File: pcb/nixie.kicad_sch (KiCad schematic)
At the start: 2 parts

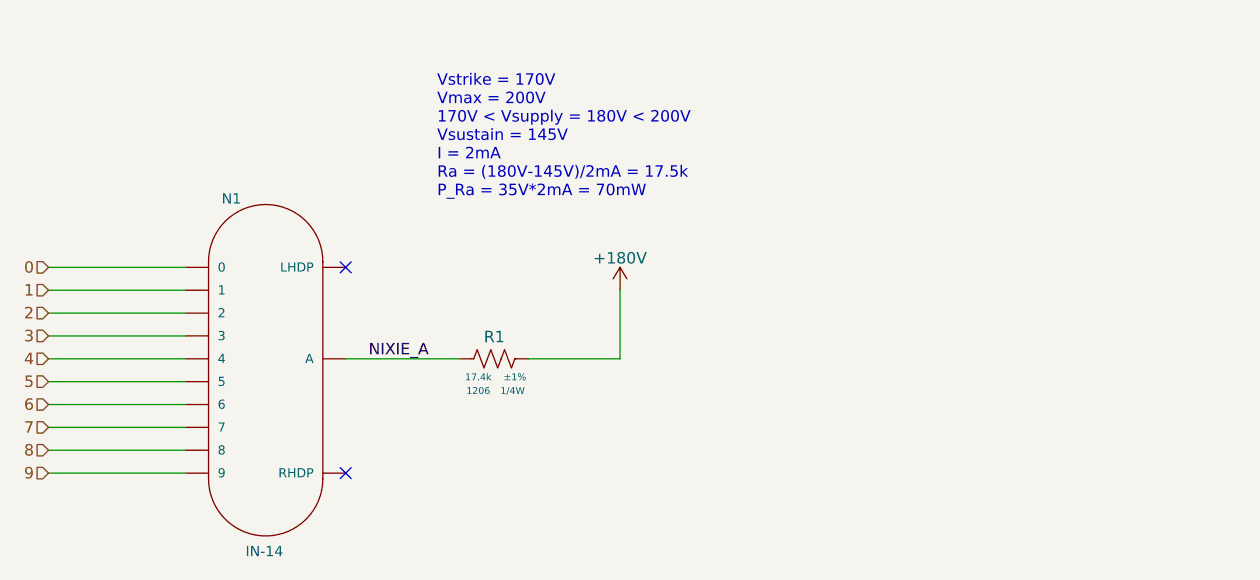
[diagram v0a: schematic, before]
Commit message: Added LSE crystal and started configuring MCU Pinout"
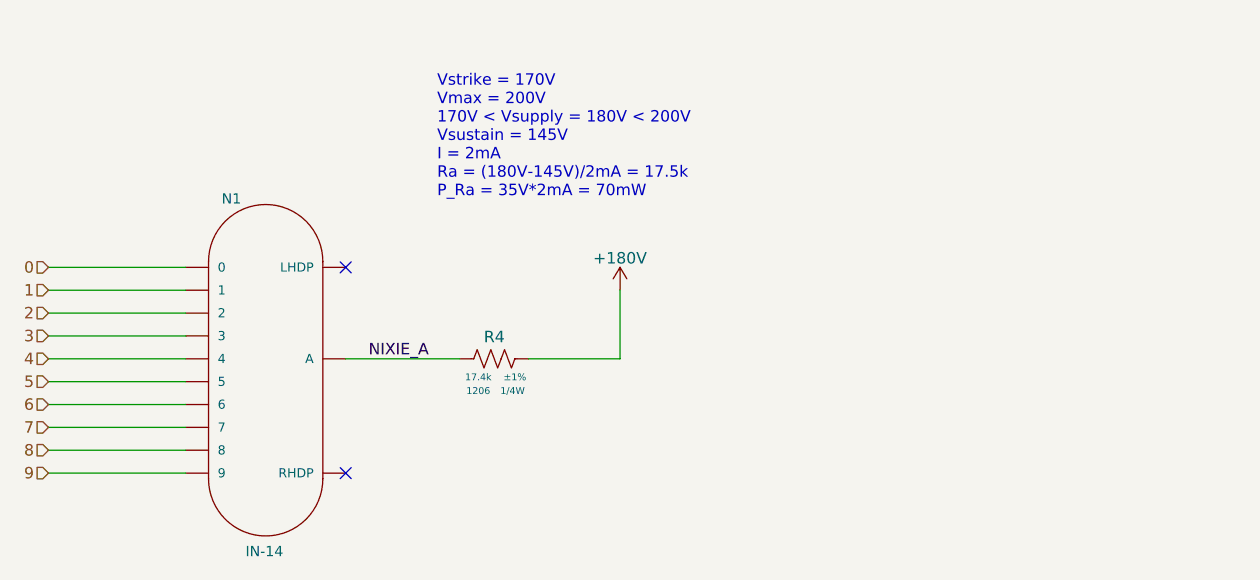
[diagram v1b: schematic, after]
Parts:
- renumbered R1 to R4
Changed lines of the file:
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@@
   (symbol (lib_id "arjun_symbols:RES_17K4_1P_1{slash}4W_1206") (at 170.18 101.6 270) (unit 1)
     (in_bom yes) (on_board yes)
-    (property "Reference" "R1" (id 0) (at 166.37 98.425 90)
+    (property "Reference" "R4" (id 0) (at 166.37 98.425 90)
       (effects (font (size 1.27 1.27)) (justify top))
     )
@@
   (symbol (lib_id "arjun_symbols:+180V") (at 180.34 93.98 0) (unit 1)
     (in_bom yes) (on_board yes)
-    (property "Reference" "#PWR06" (id 0) (at 180.34 97.79 0)
+    (property "Reference" "#PWR015" (id 0) (at 180.34 97.79 0)
       (effects (font (size 1.27 1.27)) hide)
     )

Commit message: Added 8MHz Oscillator and mapped most of the MCU pins"
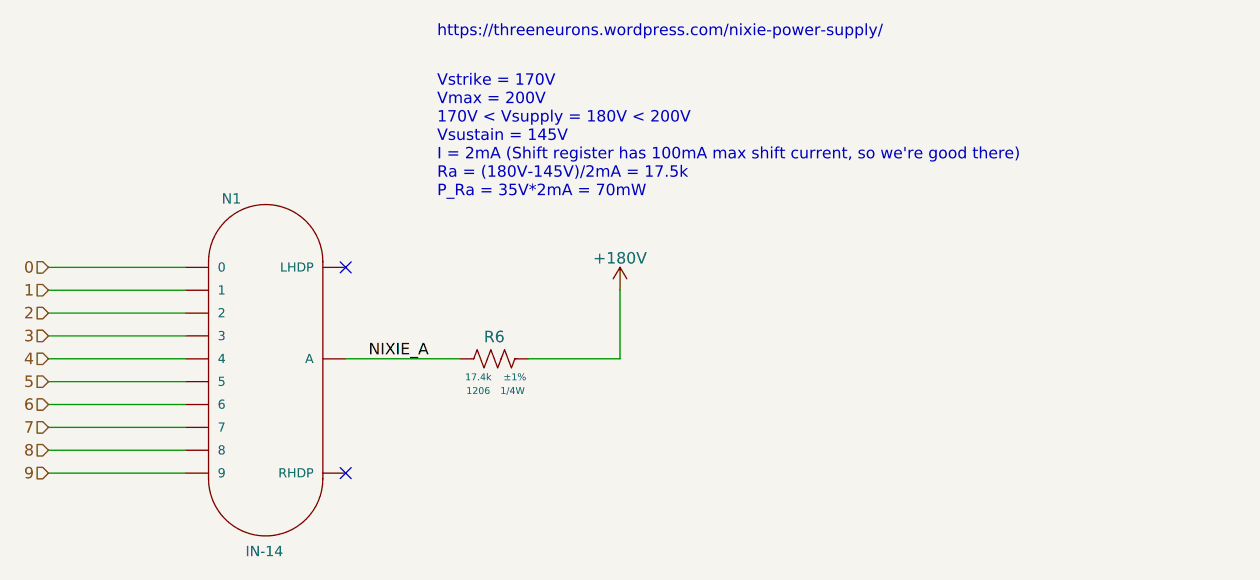
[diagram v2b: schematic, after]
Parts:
- renumbered R4 to R6
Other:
- note added: "Vstrike = 170V Vmax = 200V 170V < Vsupply = 180V < 200V Vsustain = 145V I = 2mA (Shift register has 100mA max shift current, so we're good there) Ra = (180V-145V)/2mA = 17.5k P_Ra = 35V*2mA = 70mW"
- note added: "https://threeneurons.wordpress.com/nixie-power-supply/"
- note removed: "Vstrike = 170V Vmax = 200V 170V < Vsupply = 180V < 200V Vsustain = 145V I = 2mA Ra = (180V-145V)/2mA = 17.5k P_Ra = 35V*2mA = 70mW"
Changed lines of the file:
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@@
     (stroke (width 0) (type default) (color 0 0 0 0))
   )
-  (text "Vstrike = 170V\nVmax = 200V\n170V < Vsupply = 180V < 200V\nVsustain = 145V\nI = 2mA\nRa = (180V-145V)/2mA = 17.5k\nP_Ra = 35V*2mA = 70mW"
+  (text "Vstrike = 170V\nVmax = 200V\n170V < Vsupply = 180V < 200V\nVsustain = 145V\nI = 2mA (Shift register has 100mA max shift current, so we're good there)\nRa = (180V-145V)/2mA = 17.5k\nP_Ra = 35V*2mA = 70mW"
     (at 160.02 83.82 0)
+    (effects (font (size 1.27 1.27)) (justify left bottom))
+  )
+  (text "https://threeneurons.wordpress.com/nixie-power-supply/"
+    (at 160.02 66.04 0)
     (effects (font (size 1.27 1.27)) (justify left bottom))
   )
@@
   (symbol (lib_id "arjun_symbols:RES_17K4_1P_1{slash}4W_1206") (at 170.18 101.6 270) (unit 1)
     (in_bom yes) (on_board yes)
-    (property "Reference" "R4" (id 0) (at 166.37 98.425 90)
+    (property "Reference" "R6" (id 0) (at 166.37 98.425 90)
       (effects (font (size 1.27 1.27)) (justify top))
     )
@@
   (symbol (lib_id "arjun_symbols:+180V") (at 180.34 93.98 0) (unit 1)
     (in_bom yes) (on_board yes)
-    (property "Reference" "#PWR015" (id 0) (at 180.34 97.79 0)
+    (property "Reference" "#PWR018" (id 0) (at 180.34 97.79 0)
       (effects (font (size 1.27 1.27)) hide)
     )

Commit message: Added MCU pinouts for rotary encoder
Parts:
- renumbered R6 to R9
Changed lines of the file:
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@@
   (symbol (lib_id "arjun_symbols:RES_17K4_1P_1{slash}4W_1206") (at 170.18 101.6 270) (unit 1)
     (in_bom yes) (on_board yes)
-    (property "Reference" "R6" (id 0) (at 166.37 98.425 90)
+    (property "Reference" "R9" (id 0) (at 166.37 98.425 90)
       (effects (font (size 1.27 1.27)) (justify top))
     )
@@
   (symbol (lib_id "arjun_symbols:+180V") (at 180.34 93.98 0) (unit 1)
     (in_bom yes) (on_board yes)
-    (property "Reference" "#PWR018" (id 0) (at 180.34 97.79 0)
+    (property "Reference" "#PWR031" (id 0) (at 180.34 97.79 0)
       (effects (font (size 1.27 1.27)) hide)
     )

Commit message: Added snubber DNP footprints and named nets on power page.
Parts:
- renumbered N1 to N3, R9 to R11
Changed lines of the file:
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@@
   (symbol (lib_id "arjun_symbols:RES_17K4_1P_1{slash}4W_1206") (at 170.18 101.6 270) (unit 1)
     (in_bom yes) (on_board yes)
-    (property "Reference" "R9" (id 0) (at 166.37 98.425 90)
+    (property "Reference" "R11" (id 0) (at 166.37 98.425 90)
       (effects (font (size 1.27 1.27)) (justify top))
     )
@@
   (symbol (lib_id "arjun_symbols:IN-14") (at 132.08 91.44 0) (unit 1)
     (in_bom yes) (on_board yes)
-    (property "Reference" "N1" (id 0) (at 137.16 83.82 0)
+    (property "Reference" "N3" (id 0) (at 137.16 83.82 0)
       (effects (font (size 1.143 1.143)))
     )
@@
   (symbol (lib_id "arjun_symbols:+180V") (at 180.34 93.98 0) (unit 1)
     (in_bom yes) (on_board yes)
-    (property "Reference" "#PWR031" (id 0) (at 180.34 97.79 0)
+    (property "Reference" "#PWR032" (id 0) (at 180.34 97.79 0)
       (effects (font (size 1.27 1.27)) hide)
     )

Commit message: Started layout!! 180V boost mostly laid out
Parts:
- R11: symbol arjun_symbols:RES_17K4_1P_1/4W_1206 -> arjun_symbols:RES_17K4_1P_1/4W_1206

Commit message: Added 180V clearance rules. Updated 0805 footprints to 1206 for 180V nets.
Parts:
- renumbered N3 to N8, R11 to R16
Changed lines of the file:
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@@
+		)
+	)
+	(netclass_flag ""
+		(length 2.54)
+		(shape dot)
+		(at 160.02 101.6 0)
+		(fields_autoplaced yes)
+		(effects
+			(font
+				(size 1.27 1.27)
+				(color 255 154 0 1)
+			)
+			(justify left bottom)
+		)
+		(property "Netclass" "HV"
+			(at 160.7185 99.06 0)
+			(effects
+				(font
+					(size 1.27 1.27)
+					(italic yes)
+				)
+				(justify left)
+			)
 		)
 	)
@@
 		(on_board yes)
 		(dnp no)
-		(property "Reference" "R11"
+		(property "Reference" "R16"
 			(at 166.37 98.425 90)
 			(effects
@@
 		(on_board yes)
 		(dnp no)
-		(property "Reference" "N3"
+		(property "Reference" "N8"
 			(at 137.16 83.82 0)
 			(effects
@@
 		(on_board yes)
 		(dnp no)
-		(property "Reference" "#PWR032"
+		(property "Reference" "#PWR037"
 			(at 180.34 97.79 0)
 			(effects

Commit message: Making progress on nixie tube signal routing
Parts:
- renumbered N8 to N4, R16 to R12
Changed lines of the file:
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@@
 		(on_board yes)
 		(dnp no)
-		(property "Reference" "R16"
+		(property "Reference" "R12"
 			(at 166.37 98.425 90)
 			(effects
@@
 		)
 		(instances
-			(project ""
-				(path "/962b4e87-b270-45b9-b05a-9c836fe2392e/f14ed119-44a4-4dba-a5a7-78813bb44ce1/12196d80-5ac5-4797-a091-55986a632980"
-					(reference "R16")
-					(unit 1)
-				)
-				(path "/962b4e87-b270-45b9-b05a-9c836fe2392e/f14ed119-44a4-4dba-a5a7-78813bb44ce1/32ca130f-3f8f-4402-b982-06304b6c82b9"
-					(reference "R15")
-					(unit 1)
-				)
-				(path "/962b4e87-b270-45b9-b05a-9c836fe2392e/f14ed119-44a4-4dba-a5a7-78813bb44ce1/3e78434a-9247-40fc-b232-4ebf5e38827a"
-					(reference "R12")
+			(project "STM32_Nixie"
+				(path "/962b4e87-b270-45b9-b05a-9c836fe2392e/f14ed119-44a4-4dba-a5a7-78813bb44ce1/123bc2b3-e31f-4c4e-84bd-f88f5963cf35"
+					(reference "R13")
+					(unit 1)
+				)
+				(path "/962b4e87-b270-45b9-b05a-9c836fe2392e/f14ed119-44a4-4dba-a5a7-78813bb44ce1/32b29e36-e4aa-402d-be71-eea81be37139"
+					(reference "R14")
 					(unit 1)
 				)
@@
 					(unit 1)
 				)
-				(path "/962b4e87-b270-45b9-b05a-9c836fe2392e/f14ed119-44a4-4dba-a5a7-78813bb44ce1/57e270b7-6a98-4b9f-813f-f82d4d386c31"
-					(reference "R13")
-					(unit 1)
-				)
-				(path "/962b4e87-b270-45b9-b05a-9c836fe2392e/f14ed119-44a4-4dba-a5a7-78813bb44ce1/de2dbb22-8262-4ca8-8582-8137a808f38f"
-					(reference "R14")
+				(path "/962b4e87-b270-45b9-b05a-9c836fe2392e/f14ed119-44a4-4dba-a5a7-78813bb44ce1/8d4f08ce-8f60-4112-a392-2f3cadf2f6a6"
+					(reference "R16")
+					(unit 1)
+				)
+				(path "/962b4e87-b270-45b9-b05a-9c836fe2392e/f14ed119-44a4-4dba-a5a7-78813bb44ce1/9281e11a-0024-4809-b70a-f732f328168d"
+					(reference "R12")
+					(unit 1)
+				)
+				(path "/962b4e87-b270-45b9-b05a-9c836fe2392e/f14ed119-44a4-4dba-a5a7-78813bb44ce1/d4190172-8a3a-4577-991c-8945e109fb78"
+					(reference "R15")
 					(unit 1)
 				)
@@
 		(on_board yes)
 		(dnp no)
-		(property "Reference" "N8"
+		(property "Reference" "N4"
 			(at 137.16 83.82 0)
 			(effects
@@
 		)
 		(instances
-			(project ""
-				(path "/962b4e87-b270-45b9-b05a-9c836fe2392e/f14ed119-44a4-4dba-a5a7-78813bb44ce1/12196d80-5ac5-4797-a091-55986a632980"
-					(reference "N8")
-					(unit 1)
-				)
-				(path "/962b4e87-b270-45b9-b05a-9c836fe2392e/f14ed119-44a4-4dba-a5a7-78813bb44ce1/32ca130f-3f8f-4402-b982-06304b6c82b9"
-					(reference "N7")
-					(unit 1)
-				)
-				(path "/962b4e87-b270-45b9-b05a-9c836fe2392e/f14ed119-44a4-4dba-a5a7-78813bb44ce1/3e78434a-9247-40fc-b232-4ebf5e38827a"
-					(reference "N4")
+			(project "STM32_Nixie"
+				(path "/962b4e87-b270-45b9-b05a-9c836fe2392e/f14ed119-44a4-4dba-a5a7-78813bb44ce1/123bc2b3-e31f-4c4e-84bd-f88f5963cf35"
+					(reference "N5")
+					(unit 1)
+				)
+				(path "/962b4e87-b270-45b9-b05a-9c836fe2392e/f14ed119-44a4-4dba-a5a7-78813bb44ce1/32b29e36-e4aa-402d-be71-eea81be37139"
+					(reference "N6")
 					(unit 1)
 				)
@@
 					(unit 1)
 				)
-				(path "/962b4e87-b270-45b9-b05a-9c836fe2392e/f14ed119-44a4-4dba-a5a7-78813bb44ce1/57e270b7-6a98-4b9f-813f-f82d4d386c31"
-					(reference "N5")
-					(unit 1)
-				)
-				(path "/962b4e87-b270-45b9-b05a-9c836fe2392e/f14ed119-44a4-4dba-a5a7-78813bb44ce1/de2dbb22-8262-4ca8-8582-8137a808f38f"
-					(reference "N6")
+				(path "/962b4e87-b270-45b9-b05a-9c836fe2392e/f14ed119-44a4-4dba-a5a7-78813bb44ce1/8d4f08ce-8f60-4112-a392-2f3cadf2f6a6"
+					(reference "N8")
+					(unit 1)
+				)
+				(path "/962b4e87-b270-45b9-b05a-9c836fe2392e/f14ed119-44a4-4dba-a5a7-78813bb44ce1/9281e11a-0024-4809-b70a-f732f328168d"
+					(reference "N4")
+					(unit 1)
+				)
+				(path "/962b4e87-b270-45b9-b05a-9c836fe2392e/f14ed119-44a4-4dba-a5a7-78813bb44ce1/d4190172-8a3a-4577-991c-8945e109fb78"
+					(reference "N7")
 					(unit 1)
 				)
@@
 		(on_board yes)
 		(dnp no)
-		(property "Reference" "#PWR037"
+		(property "Reference" "#PWR0114"
 			(at 180.34 97.79 0)
 			(effects
@@
 		)
 		(instances
-			(project ""
-				(path "/962b4e87-b270-45b9-b05a-9c836fe2392e/f14ed119-44a4-4dba-a5a7-78813bb44ce1/12196d80-5ac5-4797-a091-55986a632980"
-					(reference "#PWR037")
-					(unit 1)
-				)
-				(path "/962b4e87-b270-45b9-b05a-9c836fe2392e/f14ed119-44a4-4dba-a5a7-78813bb44ce1/32ca130f-3f8f-4402-b982-06304b6c82b9"
+			(project "STM32_Nixie"
+				(path "/962b4e87-b270-45b9-b05a-9c836fe2392e/f14ed119-44a4-4dba-a5a7-78813bb44ce1/123bc2b3-e31f-4c4e-84bd-f88f5963cf35"
+					(reference "#PWR032")
+					(unit 1)
+				)
+				(path "/962b4e87-b270-45b9-b05a-9c836fe2392e/f14ed119-44a4-4dba-a5a7-78813bb44ce1/32b29e36-e4aa-402d-be71-eea81be37139"
+					(reference "#PWR034")
+					(unit 1)
+				)
+				(path "/962b4e87-b270-45b9-b05a-9c836fe2392e/f14ed119-44a4-4dba-a5a7-78813bb44ce1/47fb6452-bb5d-491d-bdc1-b44524035875"
+					(reference "#PWR033")
+					(unit 1)
+				)
+				(path "/962b4e87-b270-45b9-b05a-9c836fe2392e/f14ed119-44a4-4dba-a5a7-78813bb44ce1/8d4f08ce-8f60-4112-a392-2f3cadf2f6a6"
 					(reference "#PWR036")
 					(unit 1)
 				)
-				(path "/962b4e87-b270-45b9-b05a-9c836fe2392e/f14ed119-44a4-4dba-a5a7-78813bb44ce1/3e78434a-9247-40fc-b232-4ebf5e38827a"
-					(reference "#PWR033")
-					(unit 1)
-				)
-				(path "/962b4e87-b270-45b9-b05a-9c836fe2392e/f14ed119-44a4-4dba-a5a7-78813bb44ce1/47fb6452-bb5d-491d-bdc1-b44524035875"
-					(reference "#PWR032")
-					(unit 1)
-				)
-				(path "/962b4e87-b270-45b9-b05a-9c836fe2392e/f14ed119-44a4-4dba-a5a7-78813bb44ce1/57e270b7-6a98-4b9f-813f-f82d4d386c31"
-					(reference "#PWR034")
-					(unit 1)
-				)
-				(path "/962b4e87-b270-45b9-b05a-9c836fe2392e/f14ed119-44a4-4dba-a5a7-78813bb44ce1/de2dbb22-8262-4ca8-8582-8137a808f38f"
+				(path "/962b4e87-b270-45b9-b05a-9c836fe2392e/f14ed119-44a4-4dba-a5a7-78813bb44ce1/9281e11a-0024-4809-b70a-f732f328168d"
+					(reference "#PWR0114")
+					(unit 1)
+				)
+				(path "/962b4e87-b270-45b9-b05a-9c836fe2392e/f14ed119-44a4-4dba-a5a7-78813bb44ce1/d4190172-8a3a-4577-991c-8945e109fb78"
 					(reference "#PWR035")
 					(unit 1)
